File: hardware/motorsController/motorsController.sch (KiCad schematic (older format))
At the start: 19 parts

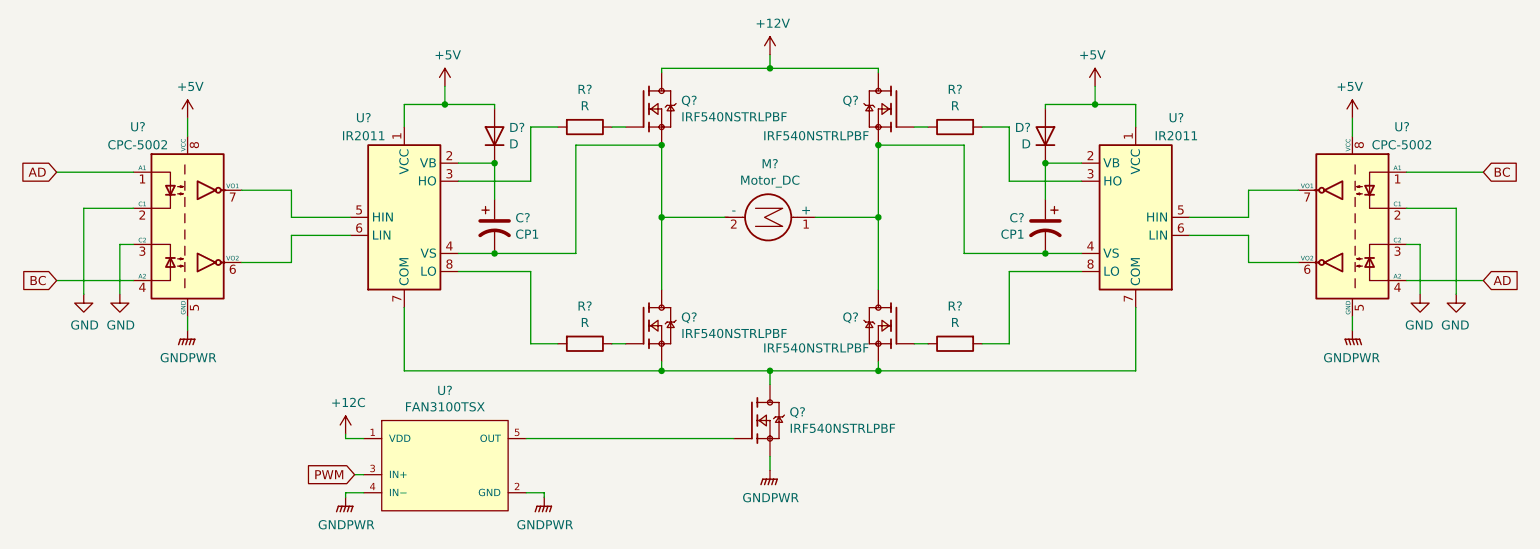
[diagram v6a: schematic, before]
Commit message: clean up the draft version of motorsController schematics
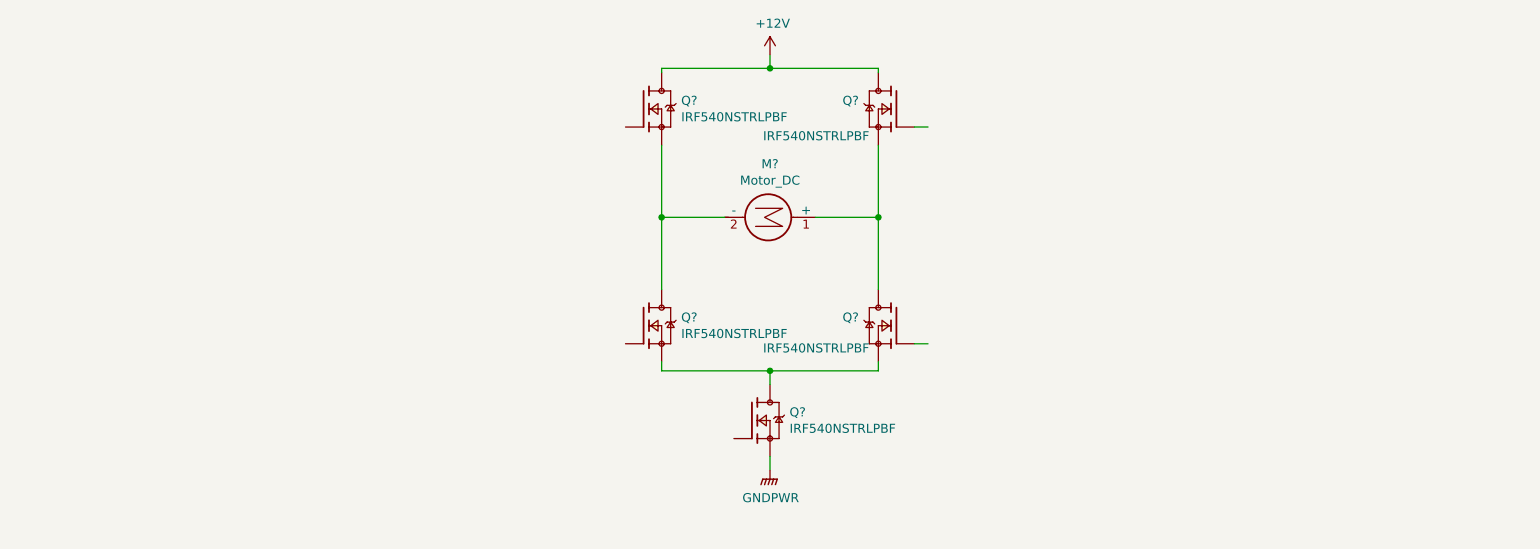
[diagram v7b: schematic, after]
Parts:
- removed C? (x2): CP1, symbol Device:CP1
- removed D? (x2): D, symbol Device:D
- removed R? (x4): R, symbol Device:R
- removed U? (x2): IR2011, symbol Driver_FET:IR2011
- removed U? (x2): CPC-5002, Package_DIP:DIP-8_W7.62mm, symbol Isolator:CPC-5002
- removed U?: FAN3100TSX, ON_Semi-527AH-0-0-*, symbol eec:FAN3100TSX
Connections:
- net labels removed: +12C, +5V, AD, BC, GND, PWM
- wire segments 95 -> 19

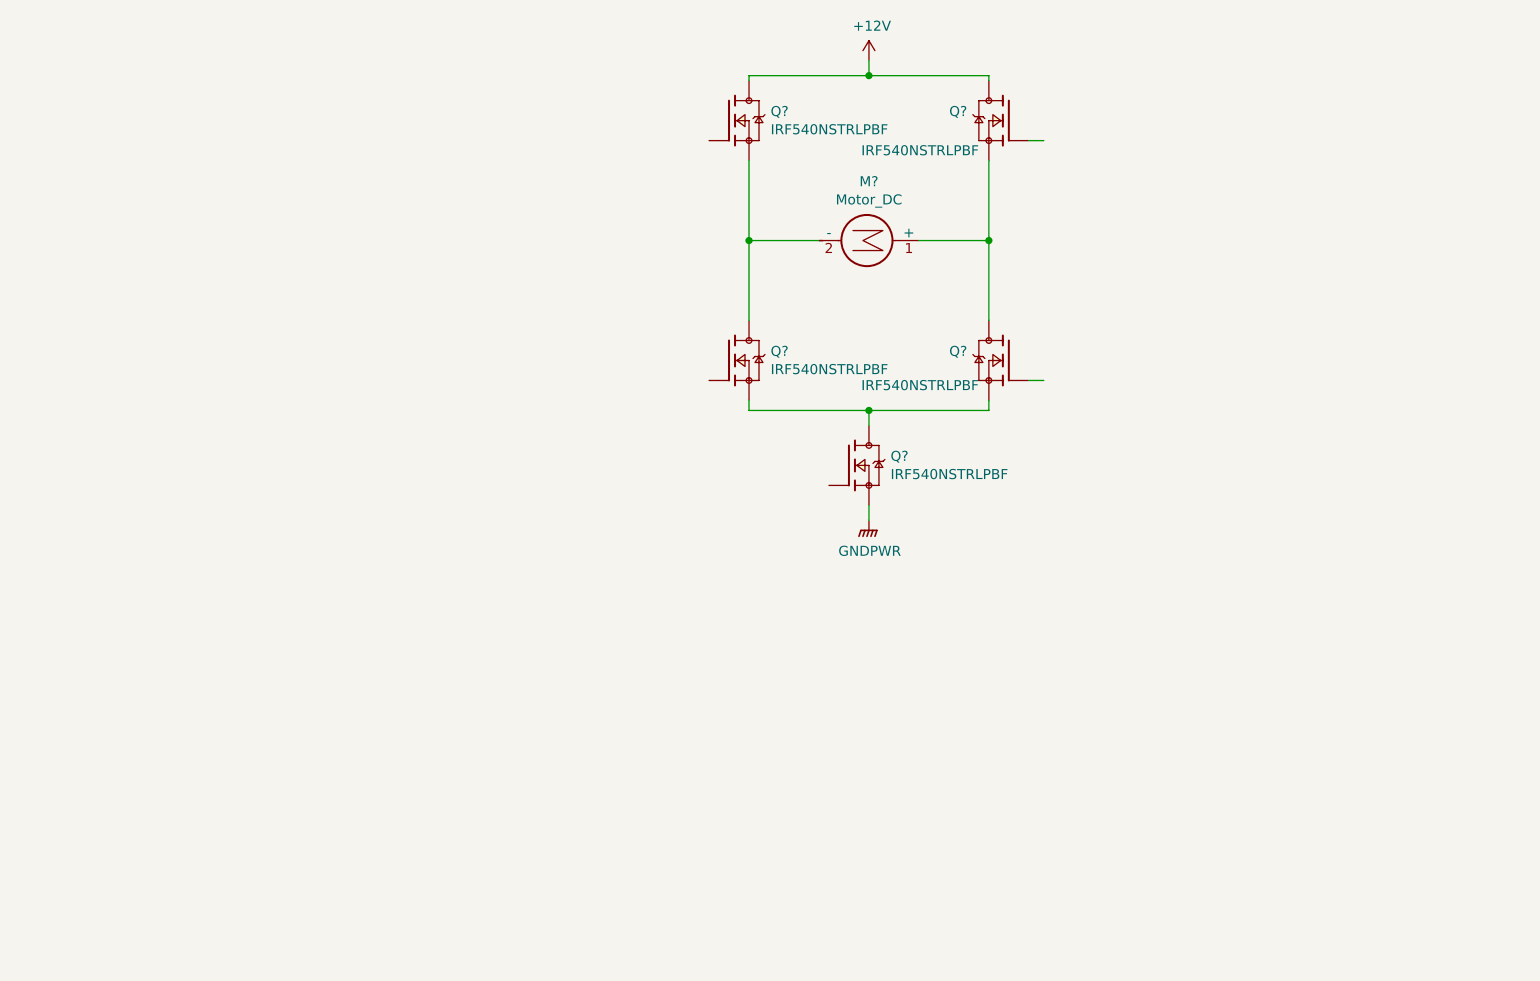
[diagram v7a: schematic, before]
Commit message: create a second draft revision of the motorsController's schematic
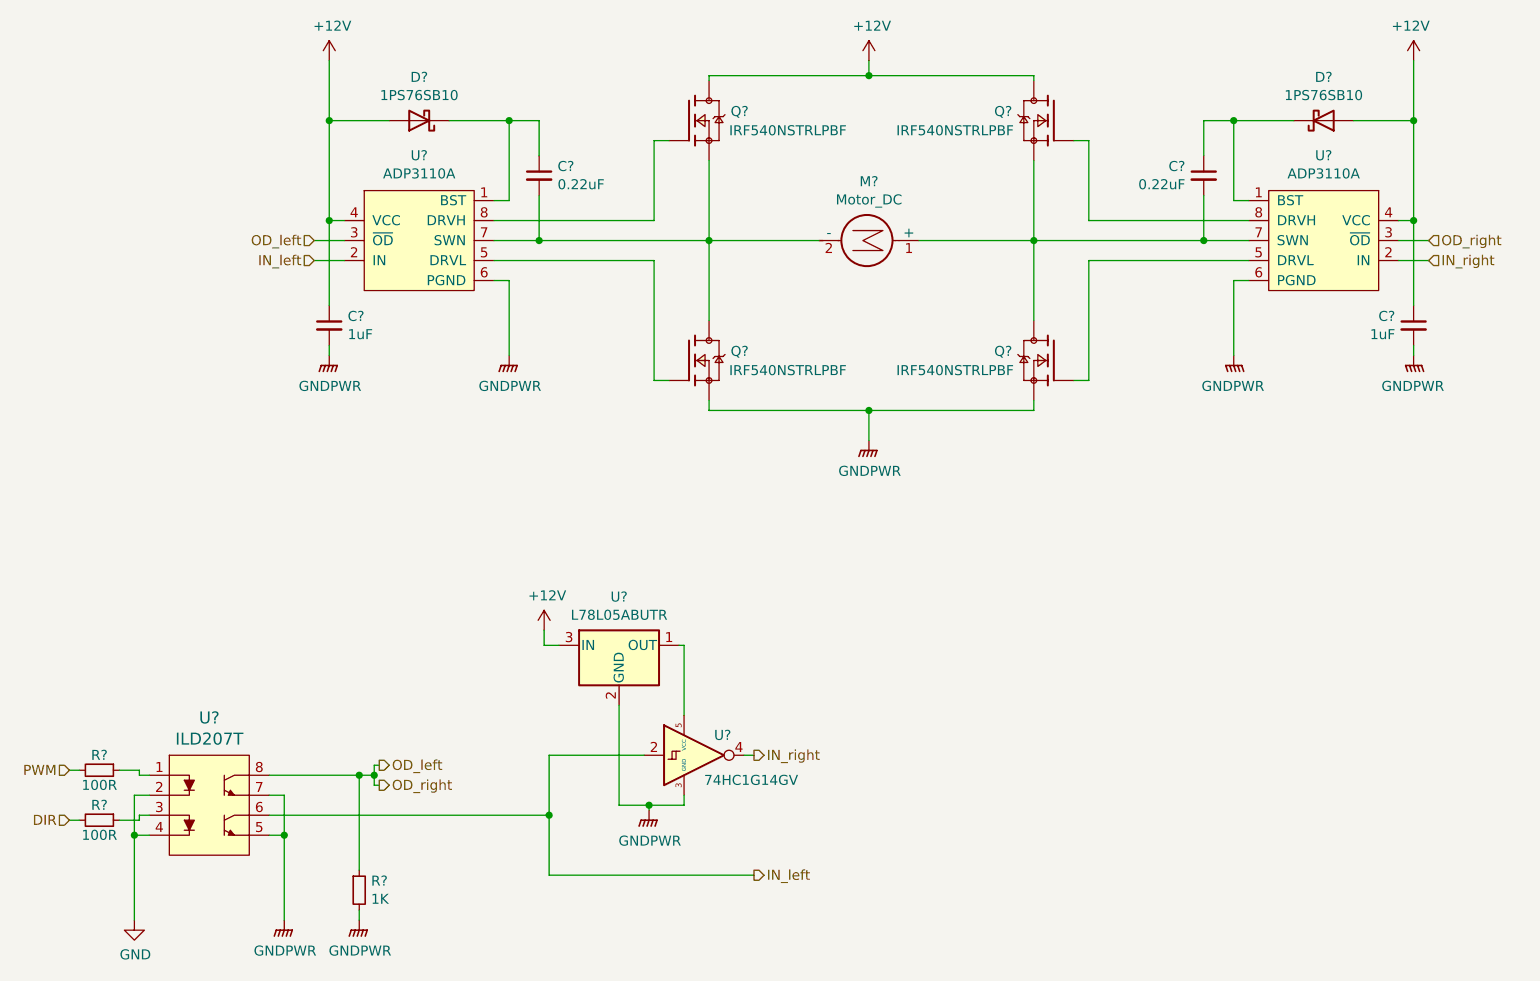
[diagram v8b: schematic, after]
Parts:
- removed Q?: IRF540NSTRLPBF, TO254P1524X483-3N, symbol IRF540NSTRLPBF:IRF540NSTRLPBF
- added C? (x2): 1uF, symbol Device:C_Small
- added C? (x2): 0.22uF, symbol Device:C_Small
- added D? (x2): 1PS76SB10, symbol Device:D_Schottky
- added R? (x2): 100R, symbol Device:R_Small
- added R?: 1K, symbol Device:R_Small
- added U?: ILD207T, digikey-footprints:SOIC-8_W3.9mm, symbol dk_Optoisolators-Transistor-Photovoltaic-Output:ILD207T
- added U? (x2): ADP3110A, symbol custom:ADP3110A
- added U?: 74HC1G14GV, symbol 74xGxx:SN74LVC1G14DBV
- added U?: L78L05ABUTR, Package_TO_SOT_SMD:SOT-89-3, symbol Regulator_Linear:L78L05_SOT89
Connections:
- net labels added: DIR, GND, IN_left, IN_right, OD_left, OD_right, PWM
- wire segments 19 -> 103
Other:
- moved on the sheet: Q?
